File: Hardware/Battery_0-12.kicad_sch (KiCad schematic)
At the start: 69 parts, among them J1 Conn_01x17, J12 Conn_01x17

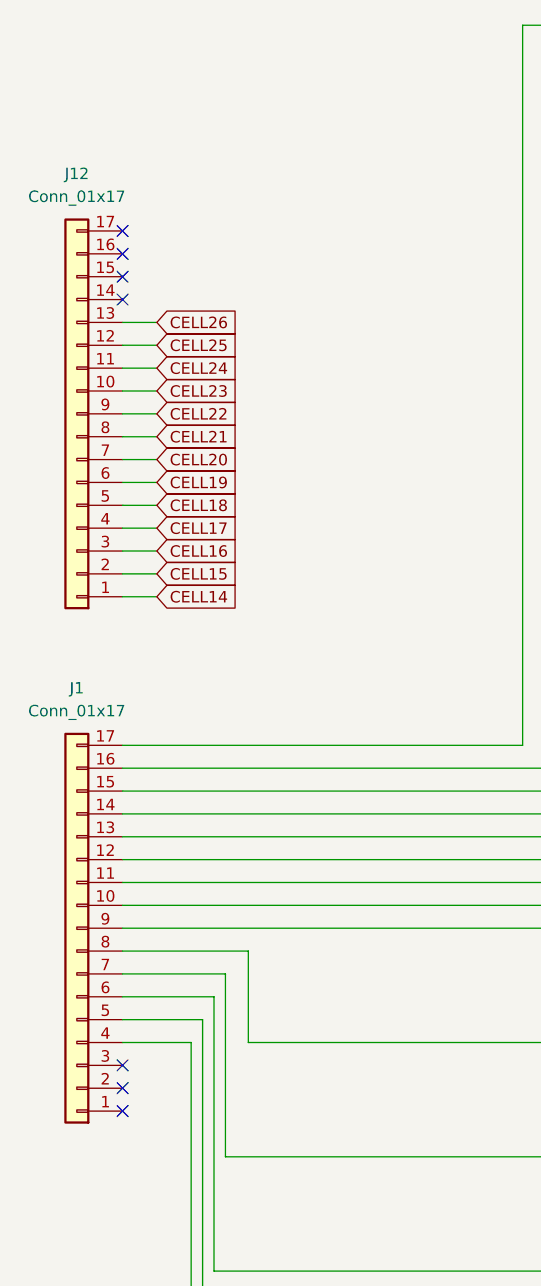
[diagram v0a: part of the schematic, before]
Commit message: Zmieniono złącza, zmieniono kondensatory na kondensatory bezpieczeństwa, poprawiono masę oraz dodano podział na hardware i software
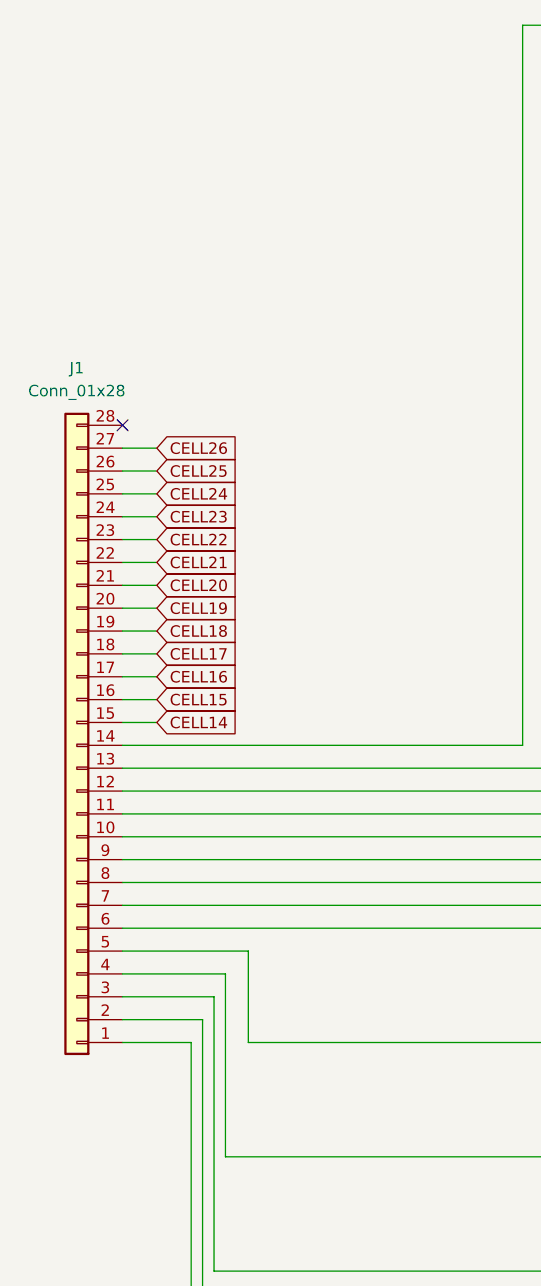
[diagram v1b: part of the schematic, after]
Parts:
- removed J1, J12: Conn_01x17, footrpint:HARWIN_B5743-117-M-L-1, symbol Connector_Generic:Conn_01x17
- added J1: Conn_01x28, footrpint:HARWIN_M80-5002842, symbol Connector_Generic:Conn_01x28
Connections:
- net Batt_Coupling: now also J1.14 (Pin_14)
- net CELL14: now also J1.15 (Pin_15)
- net CELL15: now also J1.16 (Pin_16)
- net CELL16: now also J1.17 (Pin_17)
- net CELL17: now also J1.18 (Pin_18)
- net CELL18: now also J1.19 (Pin_19)
- net CELL19: now also J1.20 (Pin_20)
- net CELL20: now also J1.21 (Pin_21)
- net CELL21: now also J1.22 (Pin_22)
- net CELL22: now also J1.23 (Pin_23)
- net CELL23: now also J1.24 (Pin_24)
- net CELL24: now also J1.25 (Pin_25)
- net CELL25: now also J1.26 (Pin_26)
- net CELL26: now also J1.27 (Pin_27)
- net GND_HV: now also J1.1 (Pin_1)
- net at BT7.2 (-), BT8.1 (+), R27.1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: now also J1.7 (Pin_7)
- net at BT8.2 (-), BT9.1 (+), R28.1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: now also J1.6 (Pin_6)
- net at BT6.2 (-), BT7.1 (+), R26.1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: now also J1.8 (Pin_8)
- net at BT1.2 (-), BT2.1 (+), R21.1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: now also J1.13 (Pin_13)
- net at BT12.2 (-), BT13.1 (+), R32.1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: now also J1.2 (Pin_2)
- net at BT11.2 (-), BT12.1 (+), R31.1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: now also J1.3 (Pin_3)
- net at BT10.2 (-), BT11.1 (+), R30.1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: now also J1.4 (Pin_4)
- net at BT10.1 (+), BT9.2 (-), R29.1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: now also J1.5 (Pin_5)
- net at BT4.2 (-), BT5.1 (+), R24.1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: now also J1.10 (Pin_10)
- net at BT5.2 (-), BT6.1 (+), R25.1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: now also J1.9 (Pin_9)
- net at BT2.2 (-), BT3.1 (+), R22.1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: now also J1.12 (Pin_12)
- net at BT3.2 (-), BT4.1 (+), R23.1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: now also J1.11 (Pin_11)
- no-connect marks 7 -> 1

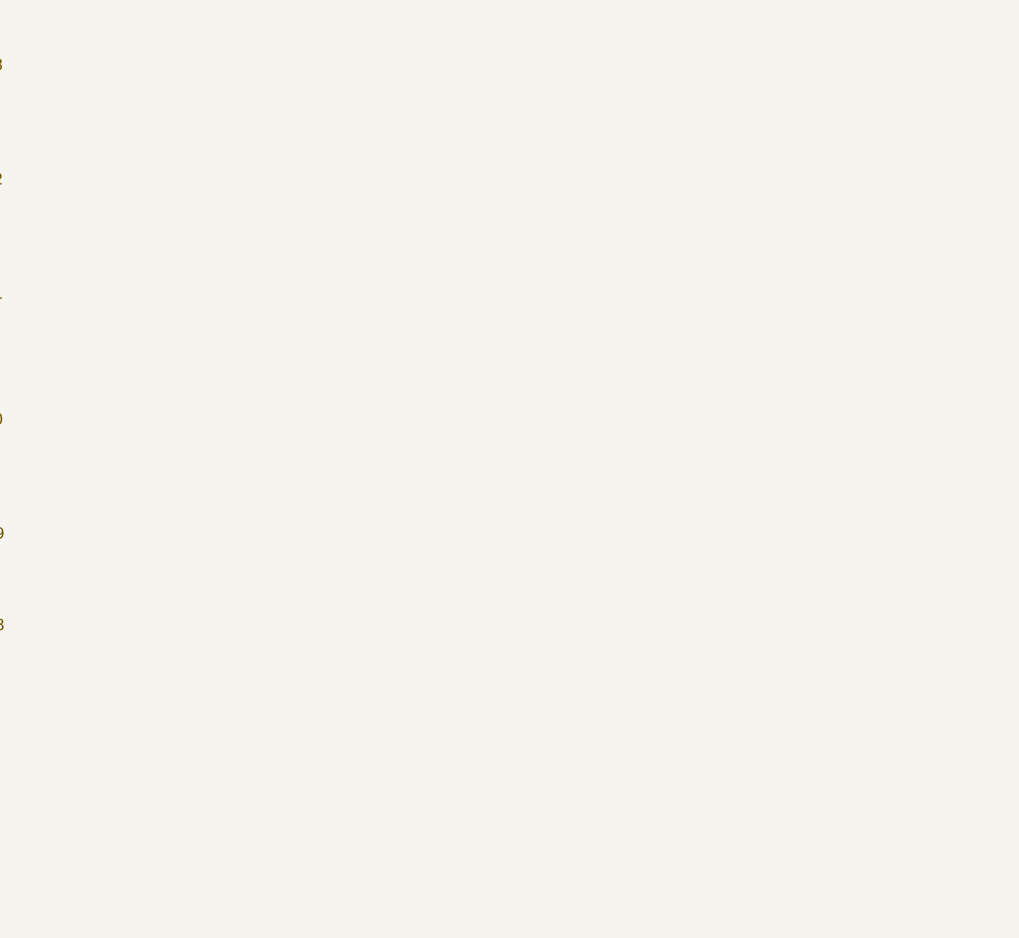
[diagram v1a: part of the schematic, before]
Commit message: Dodano diody TVS na każdej części zasilania, zmieniono bezpieczniki, podzielono bezpieczniki na bezpieczniki do prądów wewnętrznych oraz zewnętrznych,poprawiono małe błedy
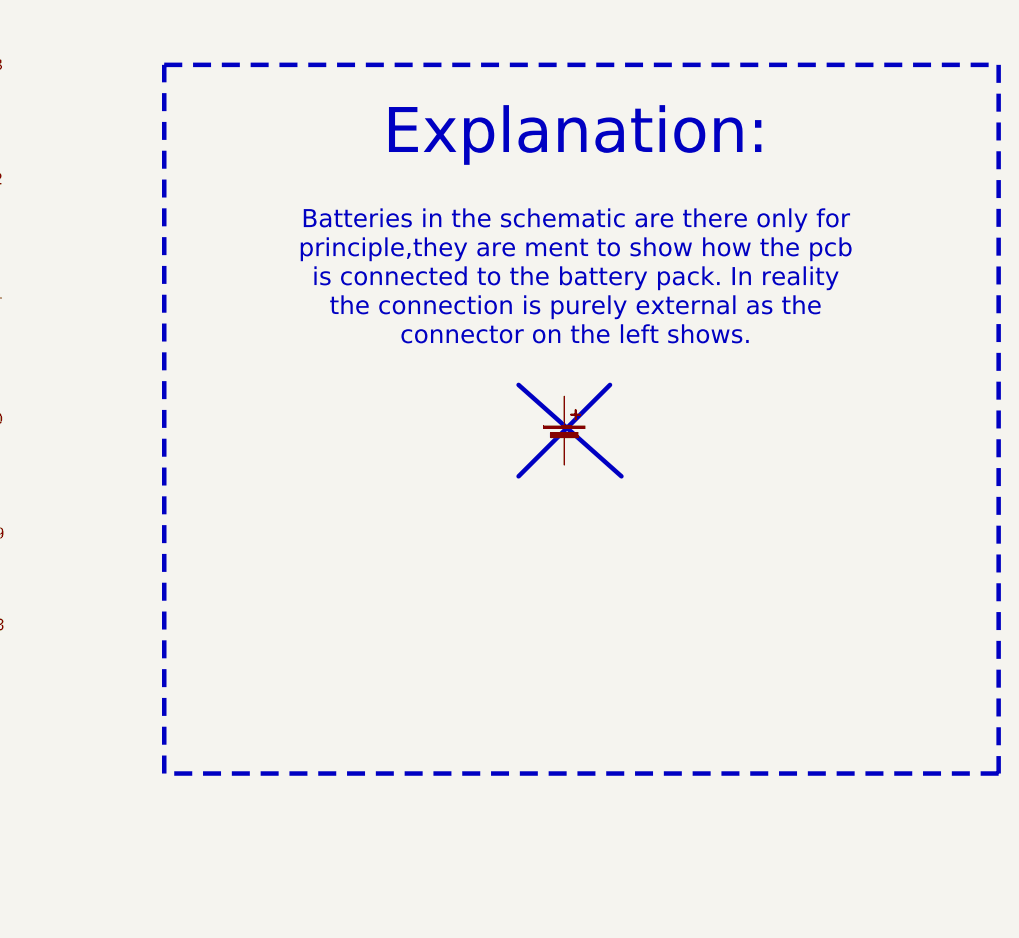
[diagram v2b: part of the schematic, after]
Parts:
- added BT27: Battery_Cell, symbol Device:Battery_Cell
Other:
- note added: "Batteries in the schematic are there only for principle,they are ment to show how the pcb is connected to the battery pack. In reality the connection is purely external as the connector on the left shows."
- note added: "Explanation:"
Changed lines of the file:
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@@
 	(generator_version "9.0")
 	(paper "A4")
+	(rectangle
+		(start 184.15 20.32)
+		(end 276.86 99.06)
+		(stroke
+			(width 0.5)
+			(type dash)
+			(color 0 0 0 1)
+		)
+		(fill
+			(type none)
+		)
+	)
+	(text "Explanation:"
+		(exclude_from_sim no)
+		(at 229.87 27.94 0)
+		(effects
+			(font
+				(size 5 5)
+				(thickness 0.625)
+				(color 0 0 0 1)
+			)
+		)
+	)
+	(text "Batteries in the schematic are there only for \nprinciple,they are ment to show how the pcb \nis connected to the battery pack. In reality\nthe connection is purely external as the\nconnector on the left shows. \n\n"
+		(exclude_from_sim no)
+		(at 229.87 45.72 0)
+		(effects
+			(font
+				(size 2 2)
+				(color 0 0 0 1)
+			)
+		)
+	)
 	(junction
 		(at 151.13 59.69)
@@
 		)
 	)
+	(polyline
+		(pts
+			(xy 223.52 55.88) (xy 234.95 66.04)
+		)
+		(stroke
+			(width 0.5)
+			(type solid)
+			(color 255 0 0 1)
+		)
+	)
 	(wire
 		(pts
@@
 		)
 	)
+	(polyline
+		(pts
+			(xy 223.52 66.04) (xy 233.68 55.88)
+		)
+		(stroke
+			(width 0.5)
+			(type solid)
+			(color 255 0 0 1)
+		)
+	)
 	(wire
 		(pts
@@
 					(unit 1)
 				)
+			)
+		)
+	)
+	(symbol
+		(lib_id "Device:Battery_Cell")
+		(at 228.6 62.23 0)
+		(unit 1)
+		(exclude_from_sim no)
+		(in_bom no)
+		(on_board no)
+		(dnp no)
+		(fields_autoplaced yes)
+		(property "Reference" "BT27"
+			(at 232.41 59.1184 0)
+			(effects
+				(font
+					(size 1.27 1.27)
+				)
+				(justify left)
+				(hide yes)
+			)
+		)
+		(property "Value" "Battery_Cell"
+			(at 232.41 61.6584 0)
+			(effects
+				(font
+					(size 1.27 1.27)
+				)
+				(justify left)
+				(hide yes)
+			)
+		)
+		(property "Footprint" ""
+			(at 228.6 60.706 90)
+			(effects
+				(font
+					(size 1.27 1.27)
+				)
+				(hide yes)
+			)
+		)
+		(property "Datasheet" "~"
+			(at 228.6 60.706 90)
+			(effects
+				(font
+					(size 1.27 1.27)
+				)
+				(hide yes)
+			)
+		)
+		(property "Description" "Single-cell battery"
+			(at 228.6 62.23 0)
+			(effects
+				(font
+					(size 1.27 1.27)
+				)
+				(hide yes)
+			)
+		)
+		(pin "1"
+		)
+		(pin "2"
+		)
+		(instances
+			(project "BMS"
+				(path "/26289bb6-56bc-4ca1-b1a2-18d58d1afdf5/329d2a9a-b359-4d8c-80ce-edb0b764c6b7/1b0b9d23-485d-43ce-ac65-957d0a9baa65"
+					(reference "BT27")
+					(unit 1)
+				)
